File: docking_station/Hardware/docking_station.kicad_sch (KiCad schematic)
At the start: 84 parts, among them IC1 VOM1271T, IC2 VOM1271T, IC3 VOM1271T, IC4 VOM1271T, IC5 VOM1271T, J1 WAGO, J2 XT60, J3 Conn_01x05_Pin, J4 SUPPLY+, J5 SUPPLY+, J6 SUPPLY-, J7 SUPPLY-, K1 RELPOL R40N-3021-85-1024, Q1 SIDR392DP-T1-GE3, Q10 DN2540N8-G, Q11 DN2540N8-G, Q12 2N7002K, Q2 SIDR392DP-T1-GE3, Q3 SIDR392DP-T1-GE3, Q4 SIDR392DP-T1-GE3, Q5 SIDR392DP-T1-GE3, Q6 SIDR392DP-T1-GE3, Q7 SIDR392DP-T1-GE3, Q8 SIDR392DP-T1-GE3, Q9 SIDR392DP-T1-GE3, U1 LTC4357MS8, U2 ACS712xLCTR-20A, U3 L78L05AB, U4 LMV321IYLT, U5 MCP6561T-E/OT, U6 MCP6561T-E/OT

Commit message: yee
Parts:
- removed J2: XT60, Connector_AMASS:AMASS_XT60PW-F_1x02_P7.20mm_Horizontal, symbol Connector_Generic:Conn_01x02
- added H1, H2, H3, H4: MountingHole_Pad, MountingHole:MountingHole_3.2mm_M3_Pad_Via, symbol Mechanical:MountingHole_Pad
- added J2: XT60, Connector_AMASS:AMASS_XT60PW-F_1x02_P7.20mm_Horizontal, symbol Connector_Generic_MountingPin:Conn_01x02_MountingPin
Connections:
- net GND: now also H1.1, H2.1, H3.1, H4.1, J2.MP (MountPin)
- net LINE_A: now also J2.1 (Pin_1)
- net LINE_B: now also J2.2 (Pin_2)

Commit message: almost finished
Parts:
- removed J4: SUPPLY+, firo_footprints:14 AWG soldering pad, symbol Connector:Conn_01x01_Pin
- removed TP23, TP24, TP25, TP26, TP5, TP6: TestPoint, TestPoint:TestPoint_Pad_D2.0mm, symbol Connector:TestPoint
- added H5, H6, H7: MountingHole_Pad, MountingHole:MountingHole_2.2mm_M2_Pad_Via, symbol Mechanical:MountingHole_Pad
- added TP10: TestPoint, TestPoint:TestPoint_Pad_D2.0mm, symbol Connector:TestPoint
- renumbered TP11 to CG1, TP12 to CG2, TP13 to CG3, TP14 to CG4, TP15 to CS1, TP16 to CS2, TP17 to CS3, TP18 to CS4, TP20 to GND1, TP21 to GND2, TP22 to GND3, TP19 to TP1, TP1 to TP2, TP2 to TP3, TP3 to TP4, TP4 to TP5, TP7 to TP6, TP8 to TP7, TP9 to TP8, TP10 to TP9
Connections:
- net GND: now also H5.1, H6.1, H7.1
- net LINE_B: now also TP10.1
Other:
- moved on the sheet: H1, H2, H3, H4

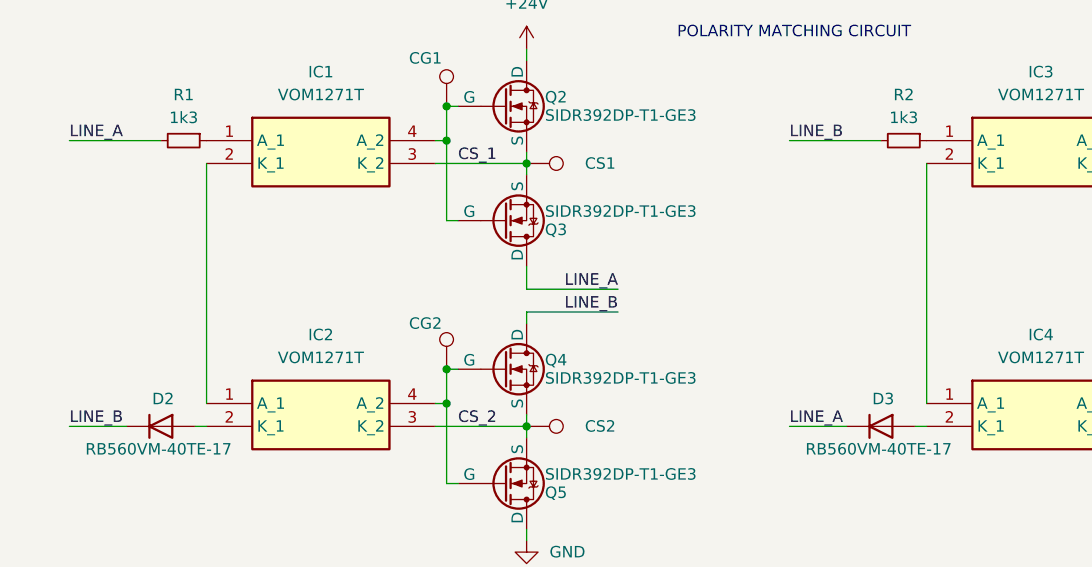
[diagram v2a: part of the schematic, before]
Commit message: MAJOR: PCB re-do begin
Revert here if needed :P
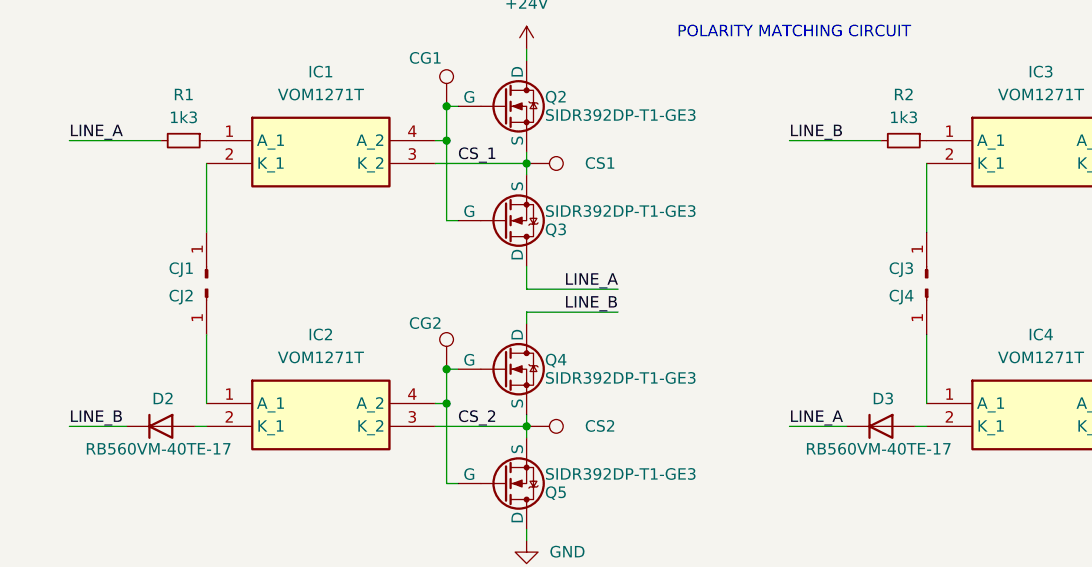
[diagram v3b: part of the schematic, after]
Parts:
- added CJ1, CJ2, CJ3, CJ4: ~, Connector_Wire:SolderWire-0.5sqmm_1x01_D0.9mm_OD2.3mm, symbol Connector:Conn_01x01_Pin
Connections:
- net at IC3.2 (K_1): now also CJ3.1 (Pin_1); no longer IC4.1 (A_1)
- net at IC2.1 (A_1): now also CJ2.1 (Pin_1); no longer IC1.2 (K_1)
- new net: CJ1.1 (Pin_1), IC1.2 (K_1)
- new net: CJ4.1 (Pin_1), IC4.1 (A_1)

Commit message: big layout updates
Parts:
- removed H5, H6, H7: MountingHole_Pad, MountingHole:MountingHole_2.2mm_M2_Pad_Via, symbol Mechanical:MountingHole_Pad
- removed J7: SUPPLY-, firo_footprints:14 AWG soldering pad, symbol Connector:Conn_01x01_Pin
- CJ1, CJ2, CJ3, CJ4: footprint Connector_Wire:SolderWire-0.5sqmm_1x01_D0.9mm_OD2.3mm -> firo_footprints:20AWG SMD
- J1: footprint (none) -> firo_footprints:WAGO 2601-3102
- J5, J6: footprint firo_footprints:14 AWG soldering pad -> firo_footprints:14 AWG THT
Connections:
- net at C7.1, R7.1, R8.1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: now also U6.4 (-); no longer U6.3 (+)
- net SUPPLY+: now reaches F1.1, J5.1 (Pin_1), TP1.1
- net at R10.1, RV2.2: now also U6.3 (+); no longer U6.4 (-)
- net at J1.1 (Pin_1): now also K1.11; no longer K1.14
- net at J1.2 (Pin_2): now also K1.14; no longer K1.11
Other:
- note added: "CH_END PULLDOWN?"
- note added: "NOT DEPLETION-MODE IN THIS SETUP"
- moved on the sheet: C7, J1, J5, J6, R8, R9, RV2, TP7

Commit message: layout complete; footprint review complete
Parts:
- removed Q10, Q11: DN2540N8-G, Package_TO_SOT_SMD:SOT-89-3, symbol Device:Q_NMOS_Depletion_DSG
- added Q10, Q11: 2N7002K, Package_TO_SOT_SMD:SOT-23, symbol Transistor_FET:2N7002K
- added R12: 10k, Resistor_SMD:R_0402_1005Metric, symbol Device:R_Small
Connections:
- net CH_END: now also R12.2
- net GND: now also R12.1
- net LINE_A: now also Q11.3 (D)
- net at C9.1, K1.A2, TP9.1: now also Q10.3 (D)
- net at IC5.4 (A_2): now also Q10.1 (G), Q11.1 (G)
- net at IC5.3 (K_2): now also Q10.2 (S), Q11.2 (S)
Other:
- note added: "Some COM LEDs?"
- note removed: "CH_END PULLDOWN?"
- note removed: "NOT DEPLETION-MODE IN THIS SETUP"

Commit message: docking station finished; 3d models & v_design added
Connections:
- net GND: no longer H1.1, H4.1
- no-connect marks 0 -> 2
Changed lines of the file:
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@@
 		(color 0 0 0 0)
 	)
+	(no_connect
+		(at 95.25 99.06)
+	)
+	(no_connect
+		(at 121.92 99.06)
+	)
 	(wire
 		(pts
@@
 	)
 	(symbol
-		(lib_id "power:GND")
-		(at 121.92 99.06 0)
-		(unit 1)
-		(exclude_from_sim no)
-		(in_bom yes)
-		(on_board yes)
-		(dnp no)
-		(fields_autoplaced yes)
-		(property "Reference" "#PWR041"
-			(at 121.92 105.41 0)
-			(effects
-				(font
-					(size 1.27 1.27)
-				)
-				(hide yes)
-			)
-		)
-		(property "Value" "GND"
-			(at 121.92 104.14 0)
-			(effects
-				(font
-					(size 1.27 1.27)
-				)
-			)
-		)
-		(property "Footprint" ""
-			(at 121.92 99.06 0)
-			(effects
-				(font
-					(size 1.27 1.27)
-				)
-				(hide yes)
-			)
-		)
-		(property "Datasheet" ""
-			(at 121.92 99.06 0)
-			(effects
-				(font
-					(size 1.27 1.27)
-				)
-				(hide yes)
-			)
-		)
-		(property "Description" "Power symbol creates a global label with name \"GND\" , ground"
-			(at 121.92 99.06 0)
-			(effects
-				(font
-					(size 1.27 1.27)
-				)
-				(hide yes)
-			)
-		)
-		(pin "1"
-		)
-		(instances
-			(project "docking_station"
-				(path "/08748f9a-6084-44ea-8855-9d9812e8dfdd"
-					(reference "#PWR041")
-					(unit 1)
-				)
-			)
-		)
-	)
-	(symbol
 		(lib_id "Comparator:MCP6561-OT")
 		(at 161.29 134.62 0)
@@
 					(unit 1)
 				)
-			)
-		)
-	)
-	(symbol
-		(lib_id "power:GND")
-		(at 95.25 99.06 0)
-		(unit 1)
-		(exclude_from_sim no)
-		(in_bom yes)
-		(on_board yes)
-		(dnp no)
-		(fields_autoplaced yes)
-		(property "Reference" "#PWR038"
-			(at 95.25 105.41 0)
-			(effects
-				(font
-					(size 1.27 1.27)
-				)
-				(hide yes)
-			)
-		)
-		(property "Value" "GND"
-			(at 95.25 104.14 0)
-			(effects
-				(font
-					(size 1.27 1.27)
-				)
-			)
-		)
-		(property "Footprint" ""
-			(at 95.25 99.06 0)
-			(effects
-				(font
-					(size 1.27 1.27)
-				)
-				(hide yes)
-			)
-		)
-		(property "Datasheet" ""
-			(at 95.25 99.06 0)
-			(effects
-				(font
-					(size 1.27 1.27)
-				)
-				(hide yes)
-			)
-		)
-		(property "Description" "Power symbol creates a global label with name \"GND\" , ground"
-			(at 95.25 99.06 0)
-			(effects
-				(font
-					(size 1.27 1.27)
-				)
-				(hide yes)
-			)
-		)
-		(pin "1"
-		)
-		(instances
-			(project ""
-				(path "/08748f9a-6084-44ea-8855-9d9812e8dfdd"
-					(reference "#PWR038")
-					(unit 1)
-				)

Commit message: Readability update begin
Added LEDs
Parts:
- removed GND3: TestPoint, TestPoint:TestPoint_Bridge_Pitch3.81mm_Drill1.3mm, symbol Connector:TestPoint
- removed TP4, TP5: TestPoint, TestPoint:TestPoint_Pad_D2.0mm, symbol Connector:TestPoint
- added D11, D12, D4, D5, D6: LED, LED_SMD:LED_0805_2012Metric, symbol Device:LED
- added R13, R14, R15: R, Resistor_SMD:R_0805_2012Metric, symbol Device:R
- R1, R2: value 1k3 -> !!
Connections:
- net +24V: now also R13.1
- net +5V: now also R14.1
- net GND: now also D4.1 (K), D5.1 (K), D6.1 (K)
- net at D3.2 (A): now also D12.1 (K); no longer IC4.2 (K_1)
- net at IC2.2 (K_1): now also D11.2 (A); no longer D2.2 (A)
- net CH_END renamed CHARGING
- net CHARGING: now also R15.1
- new net: D6.2 (A), R15.2
- new net: D5.2 (A), R14.2
- new net: D4.2 (A), R13.2
- new net: D11.1 (K), D2.2 (A)
- new net: D12.2 (A), IC4.2 (K_1)
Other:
- note added: "VALUES!!!"
- note removed: "Some COM LEDs?"
- moved on the sheet: C1, C2, C3, C4, C5, C6, C7, C8, C9, CG1, CG2, CG3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

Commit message: PCB layout, design and BOM complete; pending review
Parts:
- added C10: 100nF, Capacitor_SMD:C_0805_2012Metric, symbol Device:C_Small
- added JP2: Jumper_2_Small_Bridged, Jumper:SolderJumper-2_P1.3mm_Bridged2Bar_RoundedPad1.0x1.5mm, symbol Jumper:Jumper_2_Small_Bridged
- added Q13: 2N7002K, Package_TO_SOT_SMD:SOT-23, symbol Transistor_FET:2N7002K
- added R16: 1k, Resistor_SMD:R_0402_1005Metric, symbol Device:R_Small
- added R17, R18: 10k, Resistor_SMD:R_0402_1005Metric, symbol Device:R_Small
- added R19: 1k5, Resistor_SMD:R_0402_1005Metric, symbol Device:R_Small
- added R20: 150k, Resistor_SMD:R_0402_1005Metric, symbol Device:R_Small
- added TH1: Thermistor, Resistor_THT:R_Axial_DIN0204_L3.6mm_D1.6mm_P2.54mm_Vertical, symbol Device:Thermistor
- added U7: MCP6561T-E/OT, Package_TO_SOT_SMD:SOT-23-5, symbol Comparator:MCP6561-OT
- C4, C5, C6, C8: value 10nF -> 100nF
- C9: value 22uF -> 47uF
- D11, D12, D6: value LED -> B3V1
- D4, D5: value LED -> G2V4
- J2: footprint Connector_AMASS:AMASS_XT60PW-F_1x02_P7.20mm_Horizontal -> firo_footprints:AMASS_XT60PW-F-MP
- R1, R2: value !! -> 1k2
- R11: value 1k -> 240; footprint Resistor_SMD:R_1206_3216Metric -> Resistor_SMD:R_0805_2012Metric
- R12: value 10k -> 100k
- R13: value R -> 2k2; footprint Resistor_SMD:R_0805_2012Metric -> Resistor_SMD:R_1206_3216Metric
- R14, R15: value R -> 240
- R3: value 170 -> 240
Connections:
- net +5V: now also C10.1, R17.1, R19.1, U7.5 (V+)
- net CHARGING: now also JP2.2 (B); no longer R15.1
- net GND: now also C10.2, Q13.2 (S), R18.2, TH1.2, U7.2 (V-)
- net FLAG_LED: now reaches R10.2, TP8.1, U6.1
- net FLAG_LED: now also R15.1, R16.2; no longer JP1.1 (A)
- new net: R19.2, TH1.1, U7.4 (-)
- new net: JP1.1 (A), R16.1
- new net: Q13.1 (G), R20.2, U7.1
- new net: JP2.1 (A), Q13.3 (D)
- new net: R17.2, R18.1, R20.1, U7.3 (+)
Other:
- note added: "1k5 at 80C"
- note added: "THERMAL CHARGING CUTOFF CIRCUIT"
- note removed: "VALUES!!!"
- title: Charging Station Controller for FIRO rover -> Charging Station Controller for FIRO 2.1 rover
- moved on the sheet: C1, C4, C5, C6, C7, C8, D4, D5, D6, GND1, GND2, H1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
